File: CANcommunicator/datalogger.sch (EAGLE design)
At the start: 50 parts, among them IC1 0.1uF, IC2 1.0uF, IC3 0.1uF, IC4 0.1uF, IC5 LM2937, U1 TXB0104

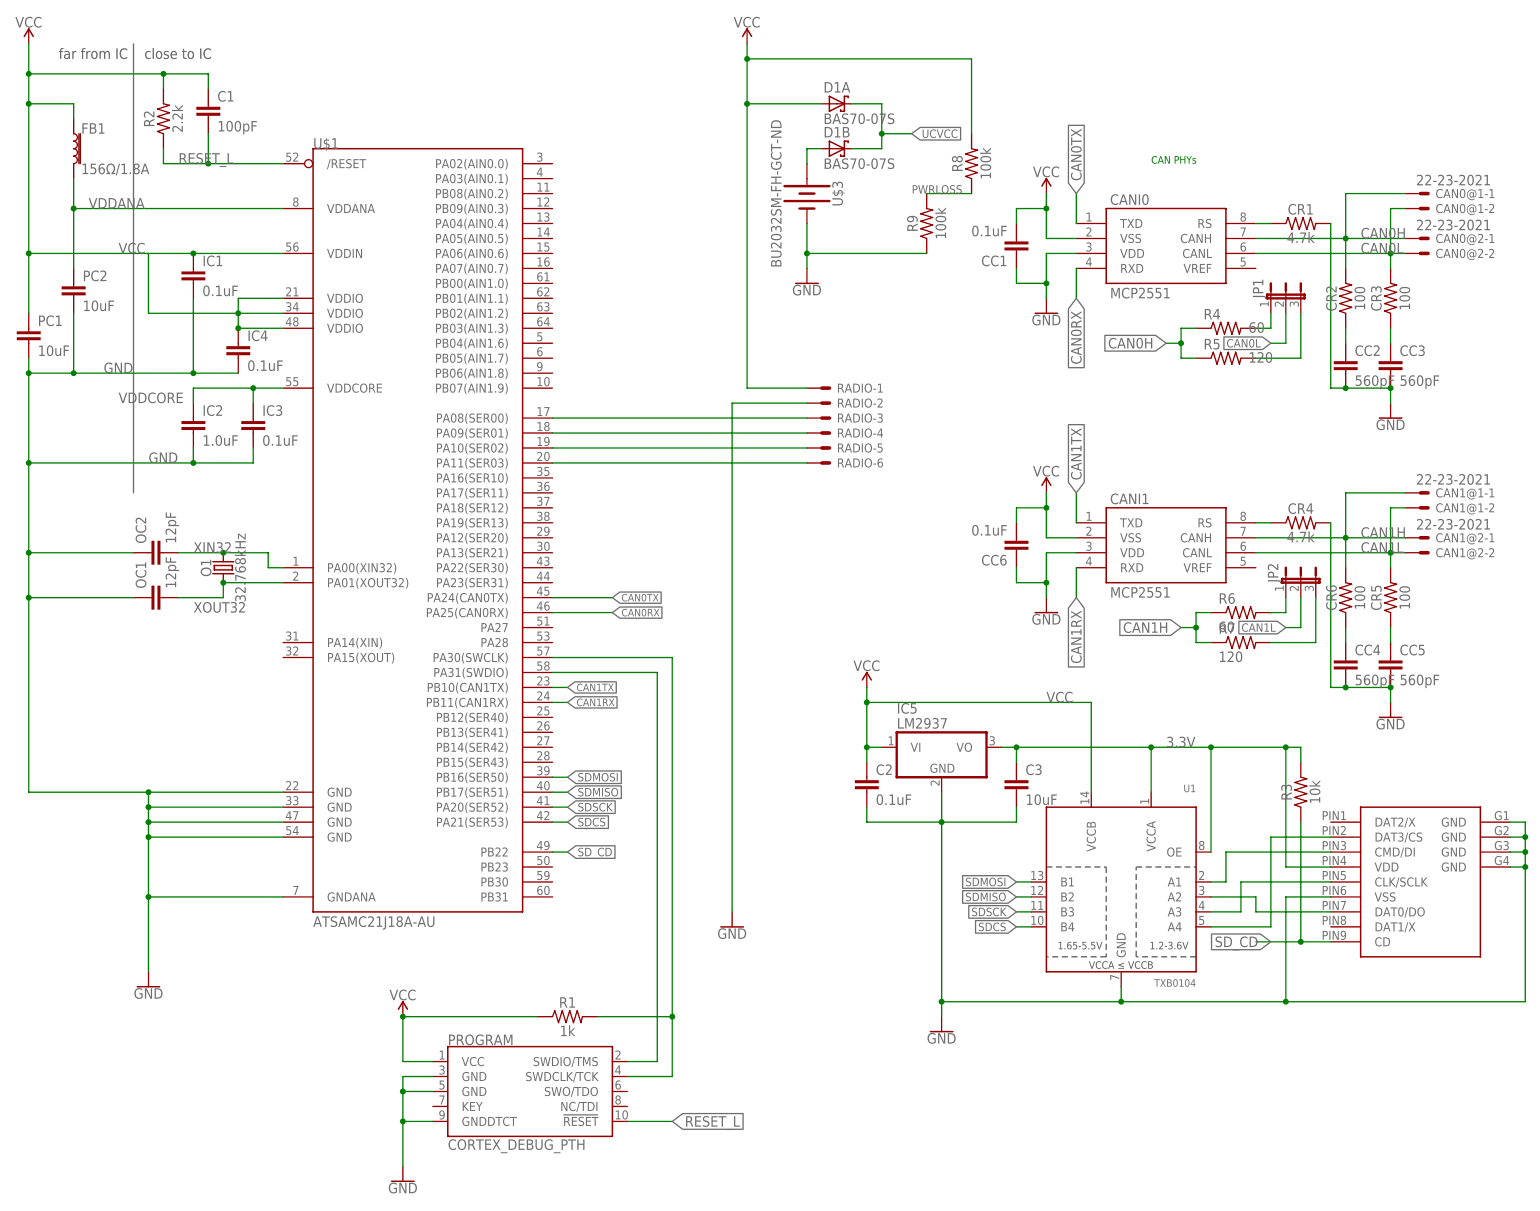
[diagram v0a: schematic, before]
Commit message: First iteration of CAN datalogger using diode RTC
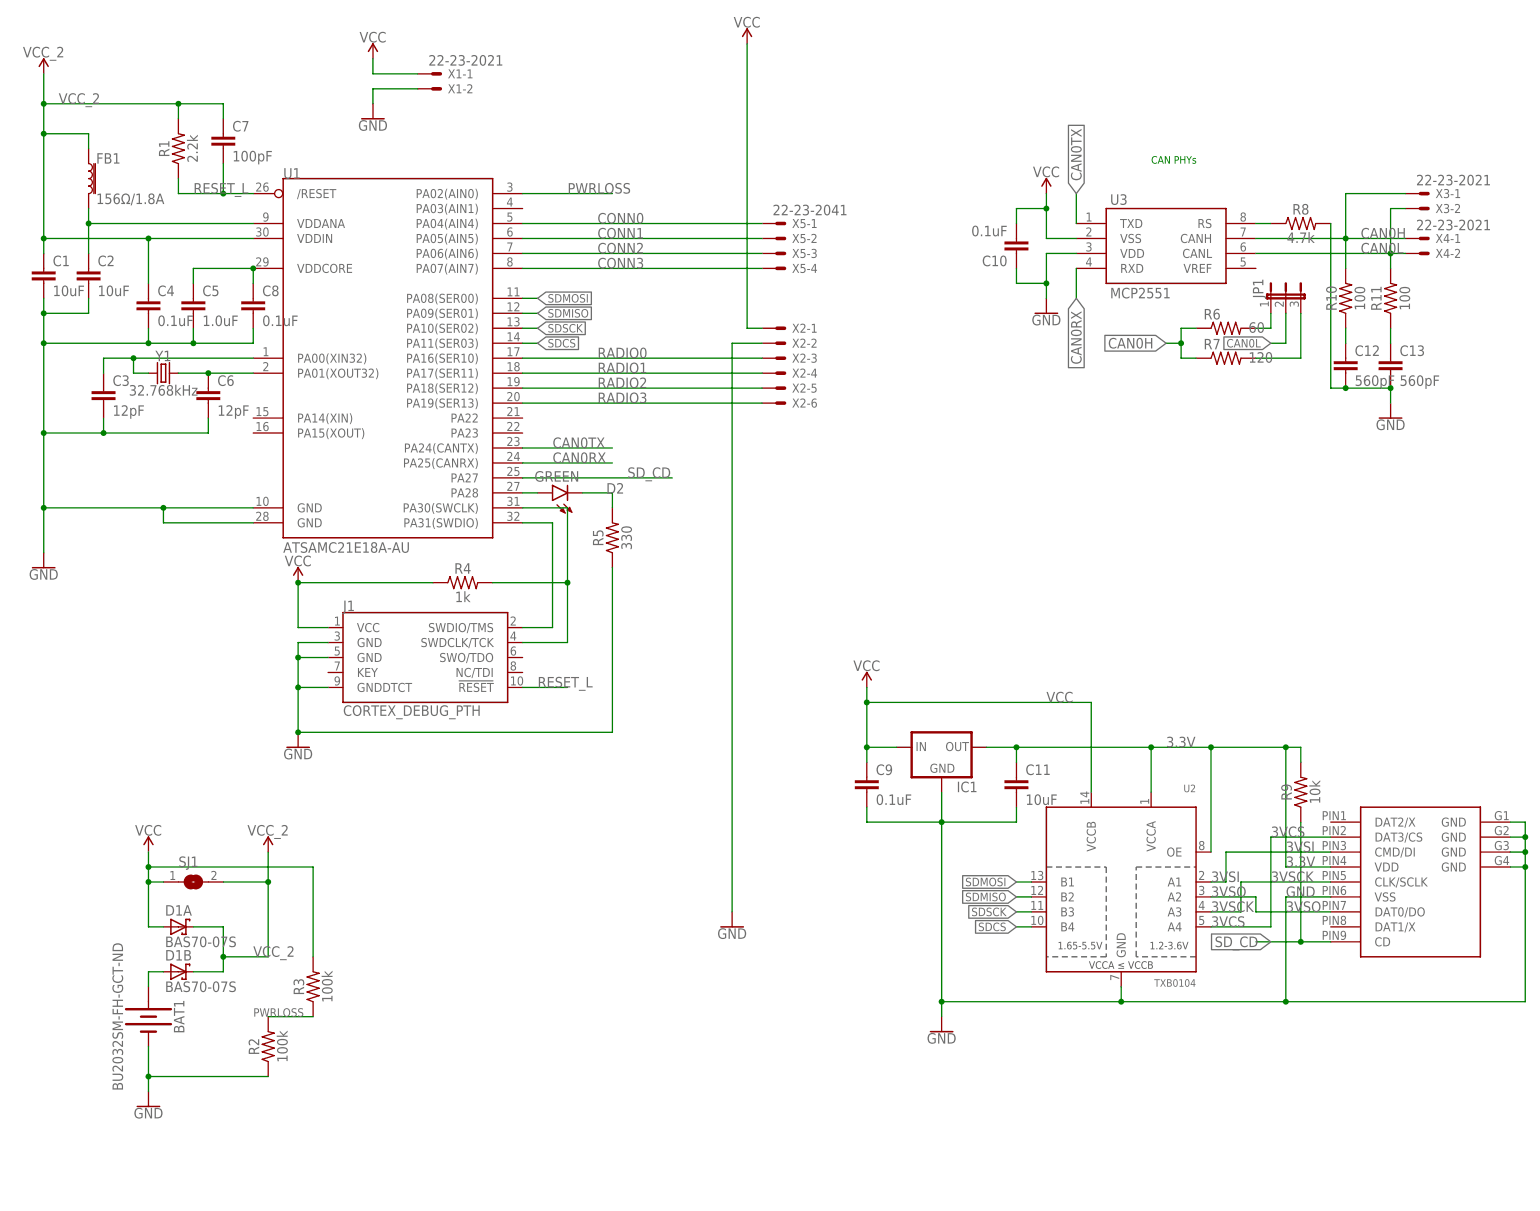
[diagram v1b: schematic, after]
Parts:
- removed CAN1@1, CAN1@2: 22-23-2021, con-molex:22-23-2021
- removed CANI1: MCP2551, SparkFun-IC-Comms:MCP2551
- removed CC4, CC5: 560pF, SparkFun-Capacitors:560PF-0603-50V-5%
- removed CC6, IC3, IC4: 0.1uF, SparkFun-Capacitors:0.1UF-0603-25V-(+80/-20%)
- removed CR1, CR4: 4.7k, SparkFun-Resistors:4.7KOHM-0603-1/10W-1%
- removed CR5, CR6: 100, SparkFun-Resistors:100OHM-0603-1/4W-5%
- removed IC2: 1.0uF, SparkFun-Capacitors:1.0UF-0603-16V-10%
- removed IC5: LM2937, linear:LM2937
- removed JP2: (no value), jumper:JP2E
- removed O1: 32.768kHz, SparkFun-Clocks:CRYSTAL-32.768KHZPTH-2X6
- removed OC1, OC2: 12pF, SparkFun-Capacitors:12PF-0603-50V-5%
- removed PC1, PC2: 10uF, SparkFun-Capacitors:10UF-0603-6.3V-20%
- removed PROGRAM: CORTEX_DEBUG_PTH, SparkFun-Connectors:CORTEX_DEBUG_PTH
- removed RADIO: (no value), con-molex:22-23-2061
- removed U$1: ATSAMC21J18A-AU, washuracing:ATSAMC21J18A-AU
- removed U$3: BU2032SM-FH-GCT-ND, washuracing:BU2032SM-FH-GCT-ND
- added BAT1: BU2032SM-FH-GCT-ND, washuracing:BU2032SM-FH-GCT-ND
- added C11: 10uF, SparkFun-Capacitors:10UF-0603-6.3V-20%
- added C4, C8, C9: 0.1uF, SparkFun-Capacitors:0.1UF-0603-25V-(+80/-20%)
- added C5: 1.0uF, SparkFun-Capacitors:1.0UF-0603-16V-10%
- added C6: 12pF, SparkFun-Capacitors:12PF-0603-50V-5%
- added C7: 100pF, SparkFun-Capacitors:100PF-0603-50V-5%
- added D2: GREEN, SparkFun-LED:LED3MM
- added J1: CORTEX_DEBUG_PTH, SparkFun-Connectors:CORTEX_DEBUG_PTH
- added SJ1: (no value), jumper:SJ
- added U2: TXB0104, SparkFun-IC-Comms:TXB0104PWR
- added X1: 22-23-2021, con-molex:22-23-2021
- added X2: (no value), con-molex:22-23-2061
- added X5: 22-23-2041, con-molex:22-23-2041
- added Y1: 32.768kHz, SparkFun-Clocks:CRYSTAL-32.768KHZPTH-2X6
- C1: value 100pF -> 10uF; device SparkFun-Capacitors:100PF-0603-50V-5% -> SparkFun-Capacitors:10UF-0603-6.3V-20%
- C2: value 0.1uF -> 10uF; device SparkFun-Capacitors:0.1UF-0603-25V-(+80/-20%) -> SparkFun-Capacitors:10UF-0603-6.3V-20%
- C3: value 10uF -> 12pF; device SparkFun-Capacitors:10UF-0603-6.3V-20% -> SparkFun-Capacitors:12PF-0603-50V-5%
- IC1: value 0.1uF -> (none); device SparkFun-Capacitors:0.1UF-0603-25V-(+80/-20%) -> v-reg:78LXX
- R1: value 1k -> 2.2k; device SparkFun-Resistors:1KOHM-0603-1/10W-1% -> SparkFun-Resistors:2.2KOHM-0603-1/10W-1%
- R2: value 2.2k -> 100k; device SparkFun-Resistors:2.2KOHM-0603-1/10W-1% -> SparkFun-Resistors:100KOHM-0603-1/10W-1%
- R3: value 10k -> 100k; device SparkFun-Resistors:10KOHM-0603-1/10W-1% -> SparkFun-Resistors:100KOHM-0603-1/10W-1%
- R4: value 60 -> 1k; device rcl:R-US_R0603 -> SparkFun-Resistors:1KOHM-0603-1/10W-1%
- R5: value 120 -> 330; device rcl:R-US_R0603 -> SparkFun-Resistors:330OHM-0603-1/10W-1%
- R8: value 100k -> 4.7k; device SparkFun-Resistors:100KOHM-0603-1/10W-1% -> SparkFun-Resistors:4.7KOHM-0603-1/10W-1%
- R9: value 100k -> 10k; device SparkFun-Resistors:100KOHM-0603-1/10W-1% -> SparkFun-Resistors:10KOHM-0603-1/10W-1%
- U1: value TXB0104 -> ATSAMC21E18A-AU; device SparkFun-IC-Comms:TXB0104PWR -> washuracing:ATSAMC21E18A-AU
- renumbered CAN0@1 to X3, CAN0@2 to X4, CANI0 to U3, CC1 to C10, CC2 to C12, CC3 to C13, CR2 to R10, CR3 to R11, U$2 to SD1
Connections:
- removed net C1HRC1: CC4.1, CR6.1
- removed net C1LRC1: CC5.1, CR5.1
- removed net C1RS1: CANI1.RS, CR4.1
- removed net CAN1H: CAN1@1-1.S, CAN1@2-1.S, CANI1.CANH, CR6.2, R6.1, R7.1
- removed net CAN1L: CAN1@1-2.S, CAN1@2-2.S, CANI1.CANL, CR5.2, JP2.2
- removed net CAN1RX: CANI1.RXD, U$1.PB11(CAN1RX)
- removed net CAN1TX: CANI1.TXD, U$1.PB10(CAN1TX)
- removed net N$1: RADIO-3.S, U$1.PA08(SER00)
- removed net N$2: RADIO-4.S, U$1.PA09(SER01)
- removed net N$3: RADIO-5.S, U$1.PA10(SER02)
- removed net N$4: RADIO-6.S, U$1.PA11(SER03)
- removed net N$6: JP2.1, R6.2
- removed net N$8: JP2.3, R7.2
- removed net N$9: D1B.A, U$3.+
- removed net UCVCC: D1A.C, D1B.C
- removed net VDDANA: FB1.2, PC2.1, U$1.VDDANA
- new net CONN0: U1.PA04(AIN4), X5-1.S
- new net CONN1: U1.PA05(AIN5), X5-2.S
- new net CONN2: U1.PA06(AIN6), X5-3.S
- new net CONN3: U1.PA07(AIN7), X5-4.S
- new net LEDA: D2.A, U1.PA28
- new net LEDC: D2.C, R5.2
- new net RADIO0: U1.PA16(SER10), X2-3.S
- new net RADIO1: U1.PA17(SER11), X2-4.S
- new net RADIO2: U1.PA18(SER12), X2-5.S
- new net RADIO3: U1.PA19(SER13), X2-6.S
- new net VBAT: BAT1.+, D1B.A
- new net VCC_2: C1.1, C4.1, C7.1, D1A.C, D1B.C, FB1.1, R1.2, SJ1.2, U1.VDDIN
- new net VDDANA1: C2.1, FB1.2, U1.VDDANA
- net 3.3V: now also C11.1, IC1.OUT, R9.2, U2.OE, U2.VCCA; no longer C3.1, IC5.VO, R3.2, U1.OE, U1.VCCA
- net 3VCS: now also U2.A4; no longer U1.A4
- net 3VSCK: now also U2.A3; no longer U1.A3
- net 3VSI: now also U2.A1; no longer U1.A1
- net 3VSO: now also U2.A2; no longer U1.A2
- net C1RS: now also R8.1; no longer CR1.1
- net CAN0H: now also R6.1, R7.1; no longer R4.1, R5.1
- net CAN0RX: now also U1.PA25(CANRX); no longer U$1.PA25(CAN0RX)
- net CAN0TX: now also U1.PA24(CANTX); no longer U$1.PA24(CAN0TX)
- net GND: now also BAT1.-, C1.2, C11.2, C4.2, C5.2, C6.2, C8.2, C9.2, IC1.GND, J1.GND@3, J1.GND@5, J1.GNDDTCT, R2.1, R5.1, R8.2, U1.GND@1, U1.GND@2, U2.GND, X1-2.S, X2-2.S; no longer CANI1.VDD, CC4.2, CC5.2, CC6.1, CR1.2, CR4.2, IC1.2, IC2.2, IC3.2, IC4.2, IC5.GND, OC1.1, OC2.1, PC1.2, PC2.2, PROGRAM.GND@3, PROGRAM.GND@5, PROGRAM.GNDDTCT, R9.1, RADIO-2.S, U$1.GND@1, U$1.GND@2, U$1.GND@3, U$1.GND@4, U$1.GNDANA, U$3.-, U1.GND
- net N$5: now also R6.2; no longer R4.2
- net N$7: now also R7.2; no longer R5.2
- net PWRLOSS: now also R2.2, R3.1, U1.PA02(AIN0); no longer R8.1, R9.2
- net RESET_L: now also C7.2, J1.!RESET, R1.1, U1./RESET; no longer C1.2, PROGRAM.!RESET, R2.1, U$1./RESET
- net SDCS: now also U1.PA11(SER03), U2.B4; no longer U$1.PA21(SER53), U1.B4
- net SDMISO: now also U1.PA09(SER01), U2.B2; no longer U$1.PB17(SER51), U1.B2
- net SDMOSI: now also U1.PA08(SER00), U2.B1; no longer U$1.PB16(SER50), U1.B1
- net SDSCK: now also U1.PA10(SER02), U2.B3; no longer U$1.PA20(SER52), U1.B3
- net SD_CD: now also R9.1, U1.PA27; no longer R3.1, U$1.PB22
- net SWDCLK: now also J1.SWDCLK/TCK, R4.2, U1.PA30(SWCLK); no longer PROGRAM.SWDCLK/TCK, R1.2, U$1.PA30(SWCLK)
- net SWDIO: now also J1.SWDIO/TMS, U1.PA31(SWDIO); no longer PROGRAM.SWDIO/TMS, U$1.PA31(SWDIO)
- net VCC: now also C9.1, IC1.IN, J1.VCC, R3.2, R4.1, SJ1.1, U2.VCCB, X1-1.S, X2-1.S; no longer C1.1, C2.1, CANI1.VSS, CC6.2, FB1.1, IC1.1, IC4.1, IC5.VI, PC1.1, PROGRAM.VCC, R1.1, R2.2, R8.2, RADIO-1.S, U$1.VDDIN, U$1.VDDIO@1, U$1.VDDIO@2, U$1.VDDIO@3, U1.VCCB
- net VDDCORE: now also C5.1, C8.1, U1.VDDCORE; no longer IC2.1, IC3.1, U$1.VDDCORE
- net XIN32: now also C3.1, U1.PA00(XIN32), Y1.1; no longer O1.2, OC2.2, U$1.PA00(XIN32)
- net XOUT32: now also C6.1, U1.PA01(XOUT32), Y1.2; no longer O1.1, OC1.2, U$1.PA01(XOUT32)
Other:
- note removed: "far from IC close to IC"
- moved on the sheet: C1, C2, C3, D1A, D1B, FB1, R1, R2, R3, R4, R5, R6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

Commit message: Diode-less battery RTC with external IC
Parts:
- removed D1: BAS70-07S, diode:BAS70-07S
- removed R2, R3: 100k, SparkFun-Resistors:100KOHM-0603-1/10W-1%
- removed SJ1: (no value), jumper:SJ
- added R12, R13: 680, SparkFun-Resistors:680OHM-0603-1/10W-5%
- added U4: DS1307Z, SparkFun-Clocks:DS1307Z
- added Y2: 32.768kHz, SparkFun-Clocks:CRYSTAL-32.768KHZPTH-2X6
- renumbered X1 to PWR, X2 to RADIO, X3 to CAN1, X4 to CAN0, X5 to LINK
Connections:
- removed net PWRLOSS: R2.2, R3.1, U1.PA02(AIN0)
- removed net VBAT: BAT1.+, D1B.A
- removed net VCC_2: C1.1, C4.1, C7.1, D1A.C, D1B.C, FB1.1, R1.2, SJ1.2, U1.VDDIN
- new net N$1: BAT1.+, U4.VBATT
- new net N$4: U4.X1, Y2.2
- new net N$6: U4.X2, Y2.1
- new net RTCSCL: R13.1, U1.PA23, U4.SCL
- new net RTCSDA: R12.1, U1.PA22, U4.SDA
- net GND: now also U4.GND; no longer R2.1
- net VCC: now also C1.1, C4.1, C7.1, FB1.1, R1.2, R12.2, R13.2, U1.VDDIN, U4.VCC; no longer D1A.A, R3.2, SJ1.1
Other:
- moved on the sheet: BAT1

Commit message: I'm an idiot
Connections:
- net GND: now also U3.VSS; no longer U3.VDD
- net VCC: now also U3.VDD; no longer U3.VSS
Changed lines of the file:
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@@
 <part name="R9" library="SparkFun-Resistors" library_urn="urn:adsk.eagle:library:532" deviceset="10KOHM" device="-0603-1/10W-1%" package3d_urn="urn:adsk.eagle:package:39650/1" value="10k"/>
 <part name="JP1" library="jumper" library_urn="urn:adsk.eagle:library:252" deviceset="JP2E" device="" package3d_urn="urn:adsk.eagle:package:15452/1"/>
-<part name="R6" library="rcl" library_urn="urn:adsk.eagle:library:334" deviceset="R-US_" device="R0603" package3d_urn="urn:adsk.eagle:package:23555/2" value="60"/>
-<part name="R7" library="rcl" library_urn="urn:adsk.eagle:library:334" deviceset="R-US_" device="R0603" package3d_urn="urn:adsk.eagle:package:23555/2" value="120"/>
+<part name="R6" library="rcl" library_urn="urn:adsk.eagle:library:334" deviceset="R-US_" device="R0603" package3d_urn="urn:adsk.eagle:package:23555/3" value="60"/>
+<part name="R7" library="rcl" library_urn="urn:adsk.eagle:library:334" deviceset="R-US_" device="R0603" package3d_urn="urn:adsk.eagle:package:23555/3" value="120"/>
 <part name="BAT1" library="washuracing" deviceset="BU2032SM-FH-GCT-ND" device=""/>
 <part name="U1" library="washuracing" deviceset="ATSAMC21E18A" device="-AU"/>
@@
 <attribute name="VALUE" x="182.88" y="183.134" size="1.778" layer="96" align="bottom-center"/>
 </instance>
-<instance part="GND7" gate="1" x="182.88" y="160.02" smashed="yes">
-<attribute name="VALUE" x="182.88" y="159.766" size="1.778" layer="96" align="top-center"/>
+<instance part="GND7" gate="1" x="177.8" y="160.02" smashed="yes">
+<attribute name="VALUE" x="177.8" y="159.766" size="1.778" layer="96" align="top-center"/>
 </instance>
 <instance part="CAN0" gate="-1" x="246.38" y="172.72" smashed="yes">
@@
 <nets>
 <net name="GND" class="1">
-<segment>
-<pinref part="U3" gate="MCP2551" pin="VDD"/>
-<wire x1="187.96" y1="170.18" x2="182.88" y2="170.18" width="0.1524" layer="91"/>
-<wire x1="182.88" y1="170.18" x2="182.88" y2="165.1" width="0.1524" layer="91"/>
-<pinref part="GND7" gate="1" pin="GND"/>
-<pinref part="C10" gate="G$1" pin="1"/>
-<wire x1="182.88" y1="165.1" x2="182.88" y2="162.56" width="0.1524" layer="91"/>
-<wire x1="177.8" y1="167.64" x2="177.8" y2="165.1" width="0.1524" layer="91"/>
-<wire x1="177.8" y1="165.1" x2="182.88" y2="165.1" width="0.1524" layer="91"/>
-<junction x="182.88" y="165.1"/>
-</segment>
 <segment>
 <pinref part="R8" gate="G$1" pin="2"/>
@@
 <junction x="157.48" y="114.3"/>
 </segment>
+<segment>
+<pinref part="C10" gate="G$1" pin="1"/>
+<pinref part="GND7" gate="1" pin="GND"/>
+<wire x1="177.8" y1="162.56" x2="177.8" y2="165.1" width="0.1524" layer="91"/>
+<pinref part="U3" gate="MCP2551" pin="VSS"/>
+<wire x1="177.8" y1="165.1" x2="177.8" y2="167.64" width="0.1524" layer="91"/>
+<wire x1="187.96" y1="172.72" x2="185.42" y2="172.72" width="0.1524" layer="91"/>
+<wire x1="185.42" y1="172.72" x2="185.42" y2="165.1" width="0.1524" layer="91"/>
+<wire x1="185.42" y1="165.1" x2="177.8" y2="165.1" width="0.1524" layer="91"/>
+<junction x="177.8" y="165.1"/>
+</segment>
 </net>
 <net name="C1RS" class="0">
@@
 <pinref part="SUPPLY6" gate="G$1" pin="VCC"/>
 <wire x1="182.88" y1="180.34" x2="182.88" y2="177.8" width="0.1524" layer="91"/>
-<pinref part="U3" gate="MCP2551" pin="VSS"/>
-<wire x1="182.88" y1="177.8" x2="182.88" y2="172.72" width="0.1524" layer="91"/>
-<wire x1="182.88" y1="172.72" x2="187.96" y2="172.72" width="0.1524" layer="91"/>
 <pinref part="C10" gate="G$1" pin="2"/>
 <wire x1="177.8" y1="175.26" x2="177.8" y2="177.8" width="0.1524" layer="91"/>
 <wire x1="177.8" y1="177.8" x2="182.88" y2="177.8" width="0.1524" layer="91"/>
+<wire x1="182.88" y1="177.8" x2="182.88" y2="170.18" width="0.1524" layer="91"/>
 <junction x="182.88" y="177.8"/>
-</segment>
-<segment>
+<pinref part="U3" gate="MCP2551" pin="VDD"/>
+<wire x1="182.88" y1="170.18" x2="187.96" y2="170.18" width="0.1524" layer="91"/>
+</segment>
+<segment>
